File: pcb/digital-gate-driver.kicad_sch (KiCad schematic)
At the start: 25 parts, among them J1 Conn_01x01_Pin, J2 Conn_01x06_Pin, J3 Conn_01x02_Socket, Q1 FDP61N20, U1 INA180A1, U2 TLV1871, U3 UC27531

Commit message: complete schematic, assign all fp
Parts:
- removed R4: ~, symbol Device:R
- removed U3: UC27531, symbol digital-gate-driver:UC27531
- added H1, H2, H3, H4: MountingHole_Pad, symbol Mechanical:MountingHole_Pad
- added JP1, JP2: Jumper_2_Small_Open, digital-gate-driver:SolderJumper-2_Open_Hooks0.8x1.8mm, symbol Jumper:Jumper_2_Small_Open
- added RV1: 2k, digital-gate-driver:PV36W201C01B00, symbol Device:R_Potentiometer
- added U4: UCC27531, symbol digital-gate-driver:UCC27531
- C1, C2, C3, C4, C5: footprint (none) -> Capacitor_SMD:C_0603_1608Metric
- D1, D2: footprint footprints:SOT323-5L -> digital-gate-driver:ESDALC6V1W5
- J1: footprint (none) -> Connector_PinHeader_2.54mm:PinHeader_2x01_P2.54mm_Vertical
- J2: footprint (none) -> Connector_PinHeader_2.54mm:PinHeader_1x06_P2.54mm_Vertical
- J3: footprint (none) -> Connector_Molex:Molex_Micro-Fit_3.0_43650-0215_1x02_P3.00mm_Vertical
- Q1: footprint (none) -> digital-gate-driver:FDP61N20
- R1, R2, R6, R7: footprint (none) -> Resistor_SMD:R_0603_1608Metric
- R3: footprint (none) -> digital-gate-driver:THT_SOCKET_RESISTOR
- R5: value ~ -> 32k; footprint (none) -> Resistor_SMD:R_0603_1608Metric
- TP1, TP2, TP3, TP4: footprint (none) -> digital-gate-driver:TP_SCOPE
- U1: footprint (none) -> digital-gate-driver:INA180A1IDBVR
- U2: footprint (none) -> digital-gate-driver:TLV1871DDFR
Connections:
- net CONDUCTION_DETECT: now also TP3.1; no longer TP3.
- net CURRENT_AMP: now also TP4.1; no longer TP4.
- net GATE_EN: now also U4.2 (IN)
- net GATE_IN: now also U4.1 (EN)
- net GND: now also TP1.2, TP2.2, TP3.2, TP4.2, H1.1, H2.1, H3.1, H4.1, RV1.2, RV1.3, U4.4 (GND); no longer TP1., TP2., TP3., TP4.
- net VCC: now also U4.3 (VDD)
- net Vdrain: now also TP1.1; no longer TP1.
- net at Q1.3 (S), R2.1: now also TP2.1; no longer TP2.
- net at Q1.2 (G), R3.2: now also JP1.2 (B)
- net Vref: now reaches R5.2, U2.3 (-)
- net Vref: now also RV1.1
- net at R3.1: now also JP2.1 (A), U4.6 (OUTH)
- new net: JP1.1 (A), JP2.2 (B), U4.5 (OUTL)
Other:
- note added: "3V3 TVS"
- note added: "DIGITAL GATE DRIVER"
- note added: "For single-ended output, solder JP2 and remove JP1"
- note added: "SECONDARY COIL CONDUCTION DETECT"
- note added: "TO FLYBACK CONVERTER"
- note added: "TO FPGA"
- note added: "TODO: Spec R6 and R7"
- note added: "TODO: spec hole sizes"
- note added: "Vref RV1 nominal 1k, Vref 0.1V nominal"
- moved on the sheet: C1, C2, C3, C4, C5, D1, D2, J1, J2, J3, Q1, R1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

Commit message: update header fp
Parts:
- J1: footprint Connector_PinHeader_2.54mm:PinHeader_2x01_P2.54mm_Vertical -> Connector_PinHeader_2.54mm:PinHeader_1x01_P2.54mm_Vertical
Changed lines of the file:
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@@
 			)
 		)
-		(property "Footprint" "Connector_PinHeader_2.54mm:PinHeader_2x01_P2.54mm_Vertical"
+		(property "Footprint" "Connector_PinHeader_2.54mm:PinHeader_1x01_P2.54mm_Vertical"
 			(at 251.46 71.12 0)
 			(effects

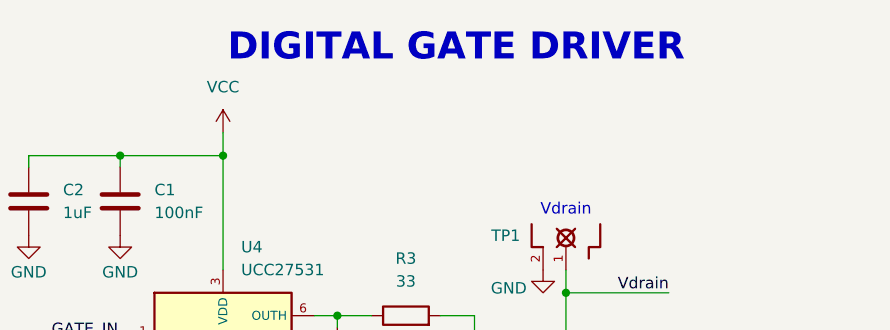
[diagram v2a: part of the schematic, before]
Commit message: update shunt resistor sizes
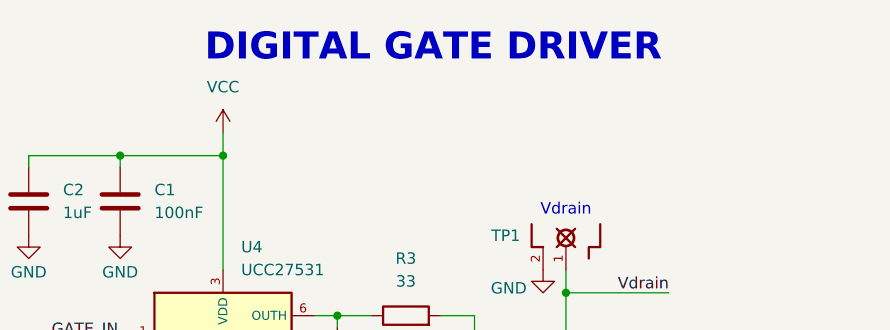
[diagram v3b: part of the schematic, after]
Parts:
- R1, R2: footprint Resistor_SMD:R_0603_1608Metric -> Resistor_SMD:R_1206_3216Metric
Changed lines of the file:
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@@
 	(text "DIGITAL GATE DRIVER"
 		(exclude_from_sim no)
-		(at 154.178 31.242 0)
+		(at 151.638 31.242 0)
 		(effects
 			(font
@@
 			)
 		)
-		(property "Footprint" "Resistor_SMD:R_0603_1608Metric"
+		(property "Footprint" "Resistor_SMD:R_1206_3216Metric"
 			(at 233.172 130.81 90)
 			(effects
@@
 			)
 		)
-		(property "Footprint" "Resistor_SMD:R_0603_1608Metric"
+		(property "Footprint" "Resistor_SMD:R_1206_3216Metric"
 			(at 164.592 80.01 90)
 			(effects

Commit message: add all footprints
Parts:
- H1, H2, H3, H4: footprint (none) -> MountingHole:MountingHole_2.5mm_Pad_Via
- U4: footprint (none) -> digital-gate-driver:UCC2753DBVT
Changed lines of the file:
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@@
 			)
 		)
-		(property "Footprint" ""
+		(property "Footprint" "MountingHole:MountingHole_2.5mm_Pad_Via"
 			(at 57.15 185.42 0)
 			(effects
@@
 			)
 		)
-		(property "Footprint" ""
+		(property "Footprint" "digital-gate-driver:UCC2753DBVT"
 			(at 128.27 53.086 0)
 			(effects
@@
 			)
 		)
-		(property "Footprint" ""
+		(property "Footprint" "MountingHole:MountingHole_2.5mm_Pad_Via"
 			(at 82.55 171.45 0)
 			(effects
@@
 			)
 		)
-		(property "Footprint" ""
+		(property "Footprint" "MountingHole:MountingHole_2.5mm_Pad_Via"
 			(at 82.55 185.42 0)
 			(effects
@@
 			)
 		)
-		(property "Footprint" ""
+		(property "Footprint" "MountingHole:MountingHole_2.5mm_Pad_Via"
 			(at 57.15 171.45 0)
 			(effects

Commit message: complete layout
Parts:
- removed J1: Conn_01x01_Pin, Connector_PinHeader_2.54mm:PinHeader_1x01_P2.54mm_Vertical, symbol Connector:Conn_01x01_Pin
- removed J3: Conn_01x02_Socket, Connector_Molex:Molex_Micro-Fit_3.0_43650-0215_1x02_P3.00mm_Vertical, symbol Connector:Conn_01x02_Socket
- added J5: Conn_01x04_Socket, digital-gate-driver:MOLEX_436500418, symbol Connector:Conn_01x04_Socket
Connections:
- net GND: now also J5.1 (Pin_1)
- net SECONDARY_SHUNT+: now also J5.4 (Pin_4)
- net VCC: now also J5.2 (Pin_2)
- net Vdrain: now also J5.3 (Pin_3)
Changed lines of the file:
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@@
 	(wire
 		(pts
-			(xy 227.33 53.34) (xy 234.95 53.34)
+			(xy 215.9 62.23) (xy 242.57 62.23)
 		)
 		(stroke
@@
 	(wire
 		(pts
+			(xy 237.49 59.69) (xy 237.49 55.88)
+		)
+		(stroke
+			(width 0)
+			(type default)
+		)
+	)
+	(wire
+		(pts
 			(xy 163.83 143.51) (xy 165.1 143.51)
 		)
@@
 	(wire
 		(pts
-			(xy 223.52 71.12) (xy 246.38 71.12)
+			(xy 215.9 64.77) (xy 242.57 64.77)
 		)
 		(stroke
@@
 	(wire
 		(pts
-			(xy 232.41 55.88) (xy 232.41 57.15)
+			(xy 240.03 57.15) (xy 240.03 67.31)
 		)
 		(stroke
@@
 	(wire
 		(pts
-			(xy 234.95 55.88) (xy 232.41 55.88)
+			(xy 242.57 57.15) (xy 240.03 57.15)
 		)
 		(stroke
@@
 	(wire
 		(pts
+			(xy 242.57 59.69) (xy 237.49 59.69)
+		)
+		(stroke
+			(width 0)
+			(type default)
+		)
+	)
+	(wire
+		(pts
 			(xy 171.45 135.89) (xy 184.15 135.89)
 		)
@@
 	)
 	(label "SECONDARY_SHUNT+"
-		(at 223.52 71.12 0)
+		(at 215.9 64.77 0)
 		(effects
 			(font
@@
 	)
 	(label "Vdrain"
-		(at 227.33 53.34 0)
+		(at 215.9 62.23 0)
 		(effects
 			(font
@@
 	)
 	(symbol
-		(lib_id "Connector:Conn_01x01_Pin")
-		(at 251.46 71.12 180)
-		(unit 1)
-		(exclude_from_sim no)
-		(in_bom yes)
-		(on_board yes)
-		(dnp no)
-		(property "Reference" "J1"
-			(at 251.46 64.77 0)
-			(effects
-				(font
-					(size 1.27 1.27)
-				)
-			)
-		)
-		(property "Value" "Conn_01x01_Pin"
-			(at 251.46 67.31 0)
-			(effects
-				(font
-					(size 1.27 1.27)
-				)
-			)
-		)
-		(property "Footprint" "Connector_PinHeader_2.54mm:PinHeader_1x01_P2.54mm_Vertical"
-			(at 251.46 71.12 0)
-			(effects
-				(font
-					(size 1.27 1.27)
-				)
-				(hide yes)
-			)
-		)
-		(property "Datasheet" "~"
-			(at 251.46 71.12 0)
-			(effects
-				(font
-					(size 1.27 1.27)
-				)
-				(hide yes)
-			)
-		)
-		(property "Description" "Generic connector, single row, 01x01, script generated"
-			(at 251.46 71.12 0)
-			(effects
-				(font
-					(size 1.27 1.27)
-				)
-				(hide yes)
-			)
-		)
-		(pin "1"
-		)
-		(instances
-			(project ""
-				(path "/89f53e89-caa4-45a9-a280-ec277a232676"
-					(reference "J1")
-					(unit 1)
-				)
-			)
-		)
-	)
-	(symbol
 		(lib_id "power:GND")
 		(at 234.95 137.16 0)
@@
 	)
 	(symbol
+		(lib_id "power:VCC")
+		(at 237.49 55.88 0)
+		(unit 1)
+		(exclude_from_sim no)
+		(in_bom yes)
+		(on_board yes)
+		(dnp no)
+		(fields_autoplaced yes)
+		(property "Reference" "#PWR34"
+			(at 237.49 59.69 0)
+			(effects
+				(font
+					(size 1.27 1.27)
+				)
+				(hide yes)
+			)
+		)
+		(property "Value" "VCC"
+			(at 237.49 50.8 0)
+			(effects
+				(font
+					(size 1.27 1.27)
+				)
+			)
+		)
+		(property "Footprint" ""
+			(at 237.49 55.88 0)
+			(effects
+				(font
+					(size 1.27 1.27)
+				)
+				(hide yes)
+			)
+		)
+		(property "Datasheet" ""
+			(at 237.49 55.88 0)
+			(effects
+				(font
+					(size 1.27 1.27)
+				)
+				(hide yes)
+			)
+		)
+		(property "Description" "Power symbol creates a global label with name \"VCC\""
+			(at 237.49 55.88 0)
+			(effects
+				(font
+					(size 1.27 1.27)
+				)
+				(hide yes)
+			)
+		)
+		(pin "1"
+		)
+		(instances
+			(project ""
+				(path "/89f53e89-caa4-45a9-a280-ec277a232676"
+					(reference "#PWR34")
+					(unit 1)
+				)
+			)
+		)
+	)
+	(symbol
 		(lib_id "power:GND")
 		(at 190.5 76.2 0)
@@
 	)
 	(symbol
+		(lib_id "Connector:Conn_01x04_Socket")
+		(at 247.65 59.69 0)
+		(unit 1)
+		(exclude_from_sim no)
+		(in_bom yes)
+		(on_board yes)
+		(dnp no)
+		(fields_autoplaced yes)
+		(property "Reference" "J5"
+			(at 248.92 59.6899 0)
+			(effects
+				(font
+					(size 1.27 1.27)
+				)
+				(justify left)
+			)
+		)
+		(property "Value" "Conn_01x04_Socket"
+			(at 248.92 62.2299 0)
+			(effects
+				(font
+					(size 1.27 1.27)
+				)
+				(justify left)
+			)
+		)
+		(property "Footprint" "digital-gate-driver:MOLEX_436500418"
+			(at 247.65 59.69 0)
+			(effects
+				(font
+					(size 1.27 1.27)
+				)
+				(hide yes)
+			)
+		)
+		(property "Datasheet" "~"
+			(at 247.65 59.69 0)
+			(effects
+				(font
+					(size 1.27 1.27)
+				)
+				(hide yes)
+			)
+		)
+		(property "Description" "Generic connector, single row, 01x04, script generated"
+			(at 247.65 59.69 0)
+			(effects
+				(font
+					(size 1.27 1.27)
+				)
+				(hide yes)
+			)
+		)
+		(pin "4"
+		)
+		(pin "3"
+		)
+		(pin "1"
+		)
+		(pin "2"
+		)
+		(instances
+			(project ""
+				(path "/89f53e89-caa4-45a9-a280-ec277a232676"
+					(reference "J5")
+					(unit 1)
+				)
+			)
+		)
+	)
+	(symbol
 		(lib_id "power:VCC")
 		(at 33.02 185.42 0)
@@
 	)
 	(symbol
-		(lib_id "Connector:Conn_01x02_Socket")
-		(at 240.03 53.34 0)
-		(unit 1)
-		(exclude_from_sim no)
-		(in_bom yes)
-		(on_board yes)
-		(dnp no)
-		(fields_autoplaced yes)
-		(property "Reference" "J3"
-			(at 241.3 53.3399 0)
-			(effects
-				(font
-					(size 1.27 1.27)
-				)
-				(justify left)
-			)
-		)
-		(property "Value" "Conn_01x02_Socket"
-			(at 241.3 55.8799 0)
-			(effects
-				(font
-					(size 1.27 1.27)
-				)
-				(justify left)
-			)
-		)
-		(property "Footprint" "Connector_Molex:Molex_Micro-Fit_3.0_43650-0215_1x02_P3.00mm_Vertical"
-			(at 240.03 53.34 0)
-			(effects
-				(font
-					(size 1.27 1.27)
-				)
-				(hide yes)
-			)
-		)
-		(property "Datasheet" "~"
-			(at 240.03 53.34 0)
-			(effects
-				(font
-					(size 1.27 1.27)
-				)
-				(hide yes)
-			)
-		)
-		(property "Description" "Generic connector, single row, 01x02, script generated"
-			(at 240.03 53.34 0)
-			(effects
-				(font
-					(size 1.27 1.27)
-				)
-				(hide yes)
-			)
-		)
-		(pin "2"
-		)
-		(pin "1"
-		)
-		(instances
-			(project ""
-				(path "/89f53e89-caa4-45a9-a280-ec277a232676"
-					(reference "J3")
-					(unit 1)
-				)
-			)
-		)
-	)
-	(symbol
 		(lib_id "power:GND")
 		(at 166.37 85.09 0)
@@
 	(symbol
 		(lib_id "power:GND")
-		(at 232.41 57.15 0)
+		(at 240.03 67.31 0)
 		(unit 1)
 		(exclude_from_sim no)
@@
 		(fields_autoplaced yes)
 		(property "Reference" "#PWR11"
-			(at 232.41 63.5 0)
+			(at 240.03 73.66 0)
 			(effects
 				(font
@@
 		)
 		(property "Value" "GND"
-			(at 232.41 62.23 0)
+			(at 240.03 72.39 0)
 			(effects
 				(font
@@
 		)
 		(property "Footprint" ""
-			(at 232.41 57.15 0)
+			(at 240.03 67.31 0)
 			(effects
 				(font
@@
 		)
 		(property "Datasheet" ""
-			(at 232.41 57.15 0)
+			(at 240.03 67.31 0)
 			(effects
 				(font
@@
 		)
 		(property "Description" "Power symbol creates a global label with name \"GND\" , ground"
-			(at 232.41 57.15 0)
+			(at 240.03 67.31 0)
 			(effects
 				(font

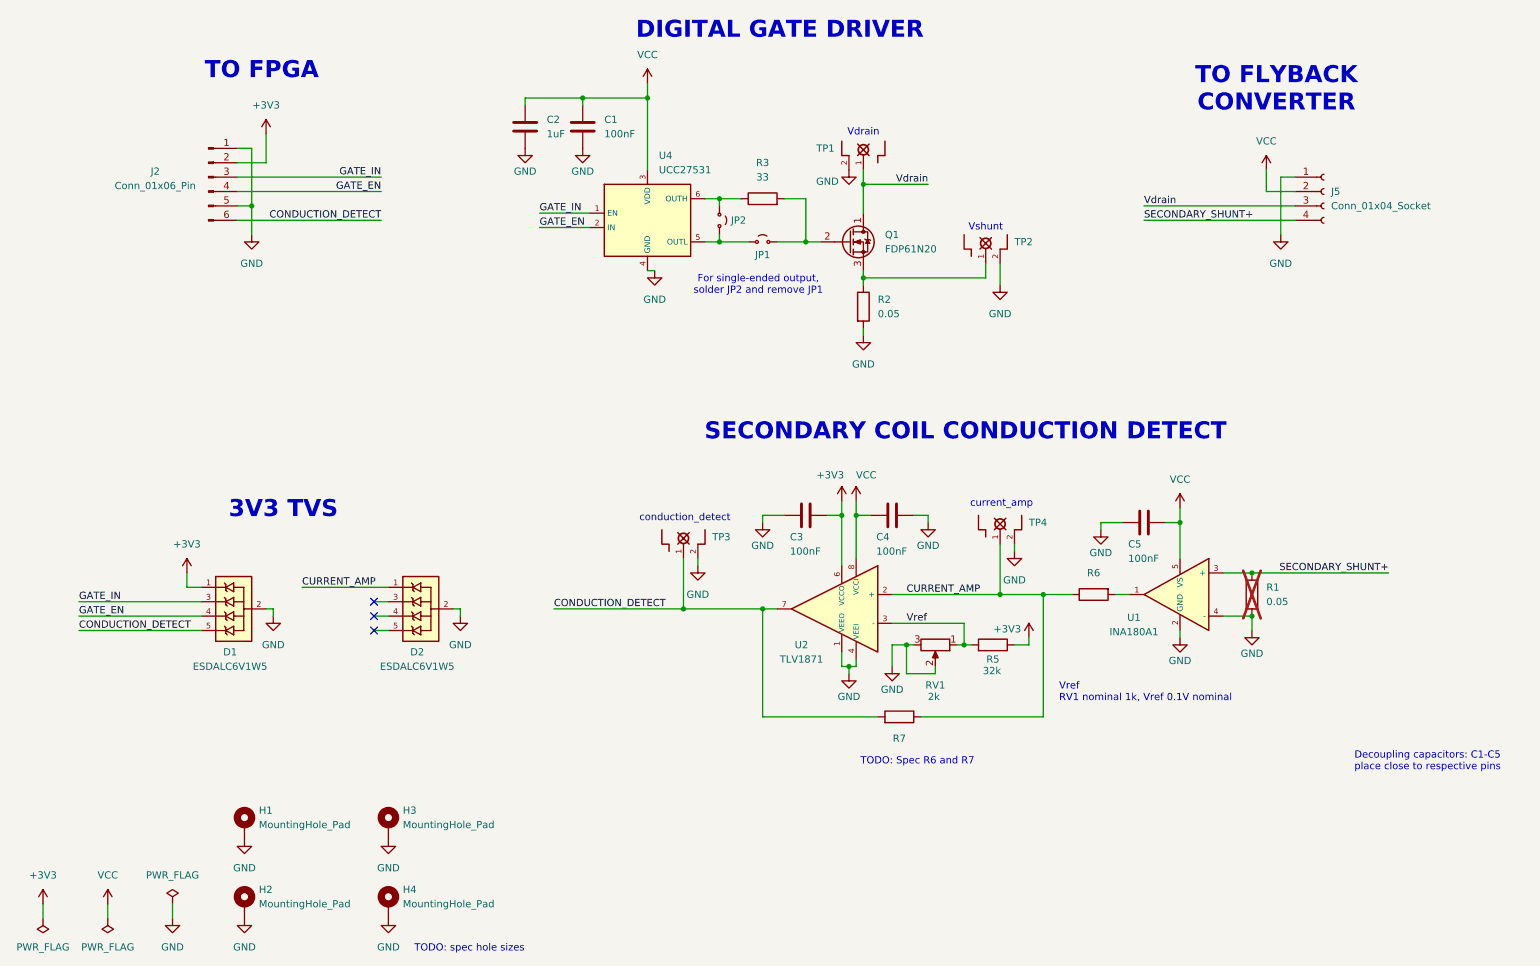
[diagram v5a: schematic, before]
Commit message: spec hysteresis resistors, update socket hole diameters
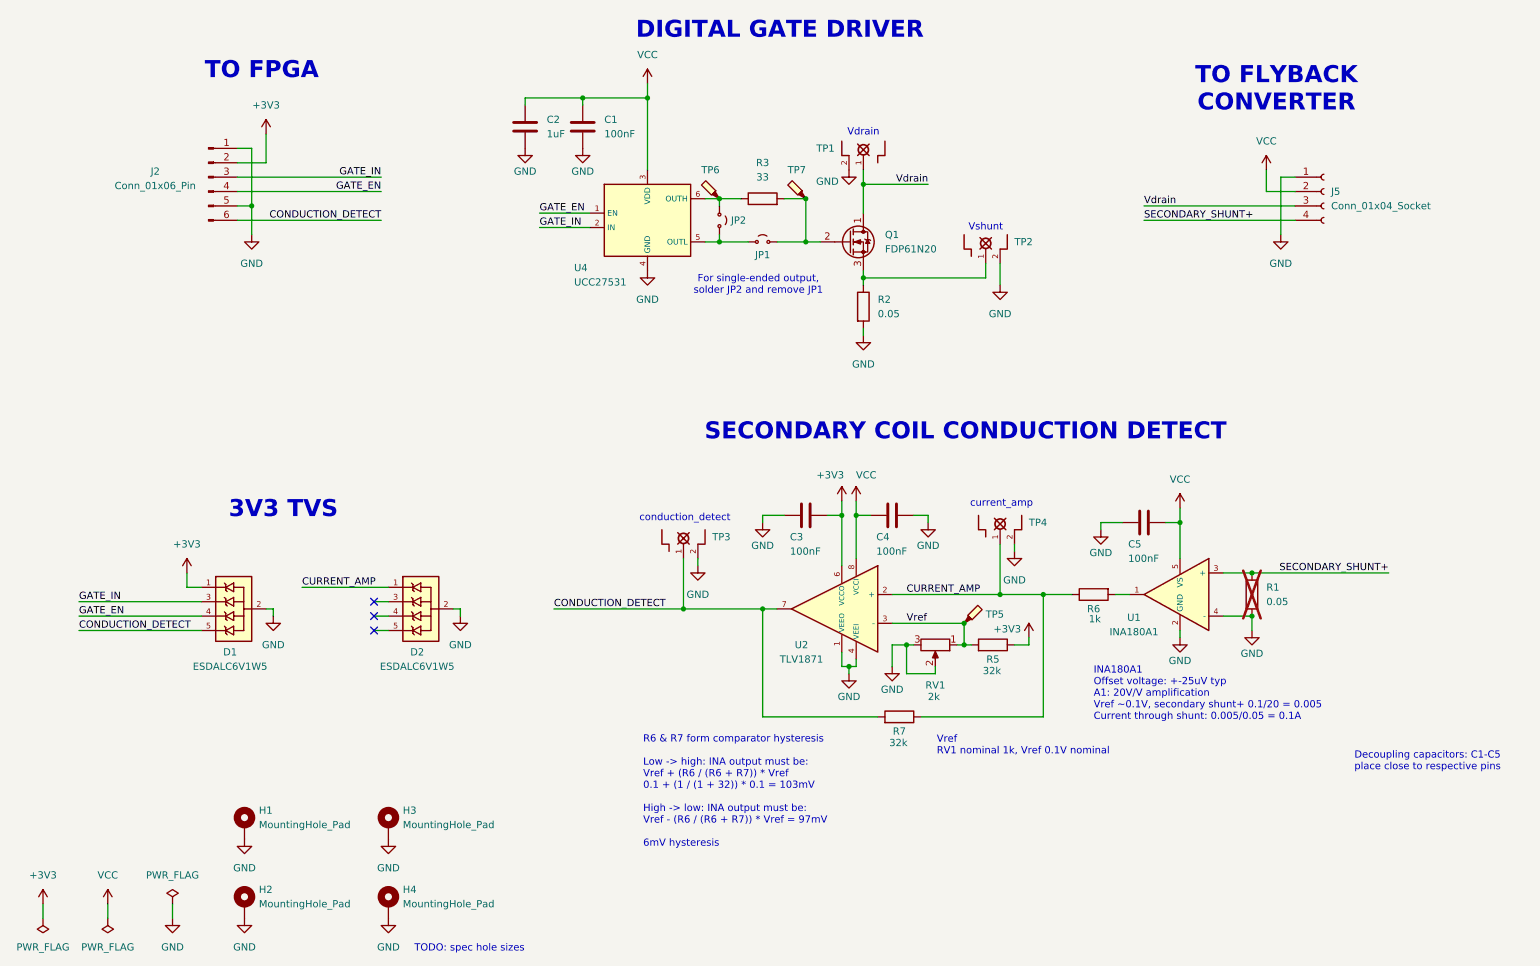
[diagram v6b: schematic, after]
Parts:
- added TP5, TP6, TP7: TestPoint_Probe, digital-gate-driver:TP_SMD, symbol Connector:TestPoint_Probe
- R6: value ~ -> 1k
- R7: value ~ -> 32k
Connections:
- net GATE_EN: now also U4.1 (EN); no longer U4.2 (IN)
- net GATE_IN: now also U4.2 (IN); no longer U4.1 (EN)
- net Vref: now also TP5.1
- net at JP2.1 (A), R3.1, U4.6 (OUTH): now also TP6.1
- net at JP1.2 (B), Q1.2 (G), R3.2: now also TP7.1
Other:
- note added: "INA180A1 Offset voltage: +-25uV typ A1: 20V/V amplification Vref ~0.1V, secondary shunt+ 0.1/20 = 0.005 Current through shunt: 0.005/0.05 = 0.1A"
- note added: "R6 & R7 form comparator hysteresis Low -> high: INA output must be: Vref + (R6 / (R6 + R7)) * Vref 0.1 + (1 / (1 + 32)) * 0.1 = 103mV High -> low: INA output must be: Vref - (R6 / (R6 + R7)) * Vref = 97mV 6mV hysteresis"
- note removed: "TODO: Spec R6 and R7"

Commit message: add final fab files
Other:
- note removed: "TODO: spec hole sizes"
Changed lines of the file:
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@@
-		)
-	)
-	(text "TODO: spec hole sizes"
-		(exclude_from_sim no)
-		(at 87.122 193.294 0)
-		(effects
-			(font
-				(size 1.27 1.27)
-			)
-			(justify left)
 		)
 	)
